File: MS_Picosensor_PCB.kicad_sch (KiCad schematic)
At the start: 24 parts, among them IC1 RASPBERRY_PI_PICO_W, J1 Conn_01x20_Socket, J2 Conn_01x20_Socket, J3 Conn_01x06_Socket, J4 Conn_01x02_Socket, J5 Conn_01x02, J6 Screw_Terminal_01x03, J7 SM04B-SRSS-TB, SW1 SW_MEC_5E, SW2 SW_MEC_5E, SW3 SW_DIP_x01

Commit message: 3v3 output
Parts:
- removed R2, R3: 1K, Resistor_THT:R_Axial_DIN0207_L6.3mm_D2.5mm_P10.16mm_Horizontal, symbol Device:R
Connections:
- net +3.3V: now also IC1.36 (3V3(OUT)), J2.5 (Pin_5); no longer IC1.37 (3V3_EN), J2.4 (Pin_4)
- new net: IC1.37 (3V3_EN), J2.4 (Pin_4)
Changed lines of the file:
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@@
-    (stroke (width 0) (type default))
-  )
-  (wire (pts (xy 132.08 125.73) (xy 132.08 128.27))
-    (stroke (width 0) (type default))
-  )
-  (wire (pts (xy 132.08 113.03) (xy 132.08 118.11))
     (stroke (width 0) (type default))
   )
@@
     (stroke (width 0) (type default))
   )
-  (wire (pts (xy 91.44 114.3) (xy 91.44 118.11))
-    (stroke (width 0) (type default))
-  )
   (wire (pts (xy 140.97 130.81) (xy 140.97 144.78))
     (stroke (width 0) (type default))
@@
     (stroke (width 0) (type default))
   )
+  (wire (pts (xy 152.4 62.23) (xy 168.91 62.23))
+    (stroke (width 0) (type default))
+  )
   (wire (pts (xy 152.4 54.61) (xy 168.91 54.61))
     (stroke (width 0) (type default))
@@
     (stroke (width 0) (type default))
   )
-  (wire (pts (xy 91.44 125.73) (xy 91.44 128.27))
-    (stroke (width 0) (type default))
-  )
   (wire (pts (xy 67.31 132.08) (xy 67.31 135.89))
     (stroke (width 0) (type default))
@@
     (stroke (width 0) (type default))
   )
-  (wire (pts (xy 152.4 62.23) (xy 168.91 62.23))
-    (stroke (width 0) (type default))
-  )
   (wire (pts (xy 29.21 31.75) (xy 29.21 35.56))
     (stroke (width 0) (type default))
@@
     (stroke (width 0) (type default))
   )
+  (wire (pts (xy 152.4 59.69) (xy 168.91 59.69))
+    (stroke (width 0) (type default))
+  )
   (wire (pts (xy 123.19 31.75) (xy 123.19 35.56))
     (stroke (width 0) (type default))
@@
     (stroke (width 0) (type default))
   )
+  (wire (pts (xy 27.94 132.08) (xy 44.45 132.08))
+    (stroke (width 0) (type default))
+  )
+  (wire (pts (xy 226.06 87.63) (xy 226.06 78.74))
+    (stroke (width 0) (type default))
+  )
+  (wire (pts (xy 36.83 80.01) (xy 53.34 80.01))
+    (stroke (width 0) (type default))
+  )
+  (wire (pts (xy 36.83 69.85) (xy 53.34 69.85))
+    (stroke (width 0) (type default))
+  )
   (wire (pts (xy 36.83 59.69) (xy 53.34 59.69))
     (stroke (width 0) (type default))
   )
-  (wire (pts (xy 27.94 132.08) (xy 44.45 132.08))
-    (stroke (width 0) (type default))
-  )
-  (wire (pts (xy 226.06 87.63) (xy 226.06 78.74))
-    (stroke (width 0) (type default))
-  )
-  (wire (pts (xy 36.83 80.01) (xy 53.34 80.01))
-    (stroke (width 0) (type default))
-  )
-  (wire (pts (xy 36.83 69.85) (xy 53.34 69.85))
-    (stroke (width 0) (type default))
-  )
   (wire (pts (xy 81.28 128.27) (xy 91.44 128.27))
     (stroke (width 0) (type default))
@@
     (stroke (width 0) (type default))
   )
-  (wire (pts (xy 152.4 59.69) (xy 168.91 59.69))
-    (stroke (width 0) (type default))
-  )
   (wire (pts (xy 152.4 97.79) (xy 168.91 97.79))
     (stroke (width 0) (type default))
@@
     (effects (font (size 1.27 1.27)) (justify left bottom))
   )
+  (label "GND" (at 36.83 95.25 0) (fields_autoplaced)
+    (effects (font (size 1.27 1.27)) (justify left bottom))
+  )
+  (label "GND" (at 36.83 57.15 0) (fields_autoplaced)
+    (effects (font (size 1.27 1.27)) (justify left bottom))
+  )
+  (label "RESET" (at 168.91 77.47 180) (fields_autoplaced)
+    (effects (font (size 1.27 1.27)) (justify right bottom))
+  )
+  (label "GND" (at 251.46 132.08 180) (fields_autoplaced)
+    (effects (font (size 1.27 1.27)) (justify right bottom))
+  )
   (label "LButton" (at 36.83 59.69 0) (fields_autoplaced)
     (effects (font (size 1.27 1.27)) (justify left bottom))
   )
-  (label "GND" (at 36.83 95.25 0) (fields_autoplaced)
-    (effects (font (size 1.27 1.27)) (justify left bottom))
-  )
-  (label "GND" (at 36.83 57.15 0) (fields_autoplaced)
-    (effects (font (size 1.27 1.27)) (justify left bottom))
-  )
-  (label "RESET" (at 168.91 77.47 180) (fields_autoplaced)
-    (effects (font (size 1.27 1.27)) (justify right bottom))
-  )
-  (label "GND" (at 251.46 132.08 180) (fields_autoplaced)
-    (effects (font (size 1.27 1.27)) (justify right bottom))
-  )
-  (label "+3.3V" (at 168.91 59.69 180) (fields_autoplaced)
-    (effects (font (size 1.27 1.27)) (justify right bottom))
-  )
   (label "GND" (at 104.14 165.1 180) (fields_autoplaced)
     (effects (font (size 1.27 1.27)) (justify right bottom))
@@
   (label "GLED" (at 27.94 118.11 0) (fields_autoplaced)
     (effects (font (size 1.27 1.27)) (justify left bottom))
+  )
+  (label "+3.3V" (at 168.91 62.23 180) (fields_autoplaced)
+    (effects (font (size 1.27 1.27)) (justify right bottom))
   )
   (symbol (lib_id "Connector:Conn_01x20_Socket") (at 31.75 74.93 0) (mirror y) (unit 1)
@@
     )
   )
-  (symbol (lib_id "power:+3.3V") (at 132.08 113.03 0) (unit 1)
-    (in_bom yes) (on_board yes) (dnp no) (fields_autoplaced)
-    (property "Reference" "#PWR07" (at 132.08 116.84 0)
-      (effects (font (size 1.27 1.27)) hide)
-    )
-    (property "Value" "+3.3V" (at 132.08 107.95 0)
-      (effects (font (size 1.27 1.27)))
-    )
-    (property "Footprint" "" (at 132.08 113.03 0)
-      (effects (font (size 1.27 1.27)) hide)
-    )
-    (property "Datasheet" "" (at 132.08 113.03 0)
-      (effects (font (size 1.27 1.27)) hide)
-    )
-    (pin "1")
-    (instances
-      (project "MS_Picosensor_PCB"
-        (path "/5da62d0f-f29a-4905-9ab2-b5107813951f"
-          (reference "#PWR07") (unit 1)
-        )
-      )
-    )
-  )
   (symbol (lib_id "Device:R") (at 48.26 132.08 90) (unit 1)
     (in_bom yes) (on_board yes) (dnp no) (fields_autoplaced)
@@
         (path "/5da62d0f-f29a-4905-9ab2-b5107813951f"
           (reference "#PWR012") (unit 1)
-        )
-      )
-    )
-  )
-  (symbol (lib_id "Device:R") (at 132.08 121.92 0) (unit 1)
-    (in_bom yes) (on_board yes) (dnp no) (fields_autoplaced)
-    (property "Reference" "R3" (at 134.62 120.65 0)
-      (effects (font (size 1.27 1.27)) (justify left))
-    )
-    (property "Value" "1K" (at 134.62 123.19 0)
-      (effects (font (size 1.27 1.27)) (justify left))
-    )
-    (property "Footprint" "Resistor_THT:R_Axial_DIN0207_L6.3mm_D2.5mm_P10.16mm_Horizontal" (at 130.302 121.92 90)
-      (effects (font (size 1.27 1.27)) hide)
-    )
-    (property "Datasheet" "~" (at 132.08 121.92 0)
-      (effects (font (size 1.27 1.27)) hide)
-    )
-    (pin "1")
-    (pin "2")
-    (instances
-      (project "MS_Picosensor_PCB"
-        (path "/5da62d0f-f29a-4905-9ab2-b5107813951f"
-          (reference "R3") (unit 1)
         )
       )
@@
     )
   )
-  (symbol (lib_id "power:+3.3V") (at 91.44 114.3 0) (unit 1)
-    (in_bom yes) (on_board yes) (dnp no) (fields_autoplaced)
-    (property "Reference" "#PWR06" (at 91.44 118.11 0)
-      (effects (font (size 1.27 1.27)) hide)
-    )
-    (property "Value" "+3.3V" (at 91.44 109.22 0)
-      (effects (font (size 1.27 1.27)))
-    )
-    (property "Footprint" "" (at 91.44 114.3 0)
-      (effects (font (size 1.27 1.27)) hide)
-    )
-    (property "Datasheet" "" (at 91.44 114.3 0)
-      (effects (font (size 1.27 1.27)) hide)
-    )
-    (pin "1")
-    (instances
-      (project "MS_Picosensor_PCB"
-        (path "/5da62d0f-f29a-4905-9ab2-b5107813951f"
-          (reference "#PWR06") (unit 1)
-        )
-      )
-    )
-  )
   (symbol (lib_id "power:GND") (at 97.79 146.05 0) (unit 1)
     (in_bom yes) (on_board yes) (dnp no) (fields_autoplaced)
@@
         )
       )
-    )
-  )
-  (symbol (lib_id "Device:R") (at 91.44 121.92 0) (unit 1)
-    (in_bom yes) (on_board yes) (dnp no) (fields_autoplaced)
-    (property "Reference" "R2" (at 93.98 120.65 0)
-      (effects (font (size 1.27 1.27)) (justify left))
-    )
-    (property "Value" "1K" (at 93.98 123.19 0)
-      (effects (font (size 1.27 1.27)) (justify left))
-    )
-    (property "Footprint" "Resistor_THT:R_Axial_DIN0207_L6.3mm_D2.5mm_P10.16mm_Horizontal" (at 89.662 121.92 90)
-      (effects (font (size 1.27 1.27)) hide)
-    )
-    (property "Datasheet" "~" (at 91.44 121.92 0)
-      (effects (font (size 1.27 1.27)) hide)
-    )
-    (pin "1")
-    (pin "2")
-    (instances
-      (project "MS_Picosensor_PCB"
-        (path "/5da62d0f-f29a-4905-9ab2-b5107813951f"
-          (reference "R2") (unit 1)
-        )
-      )

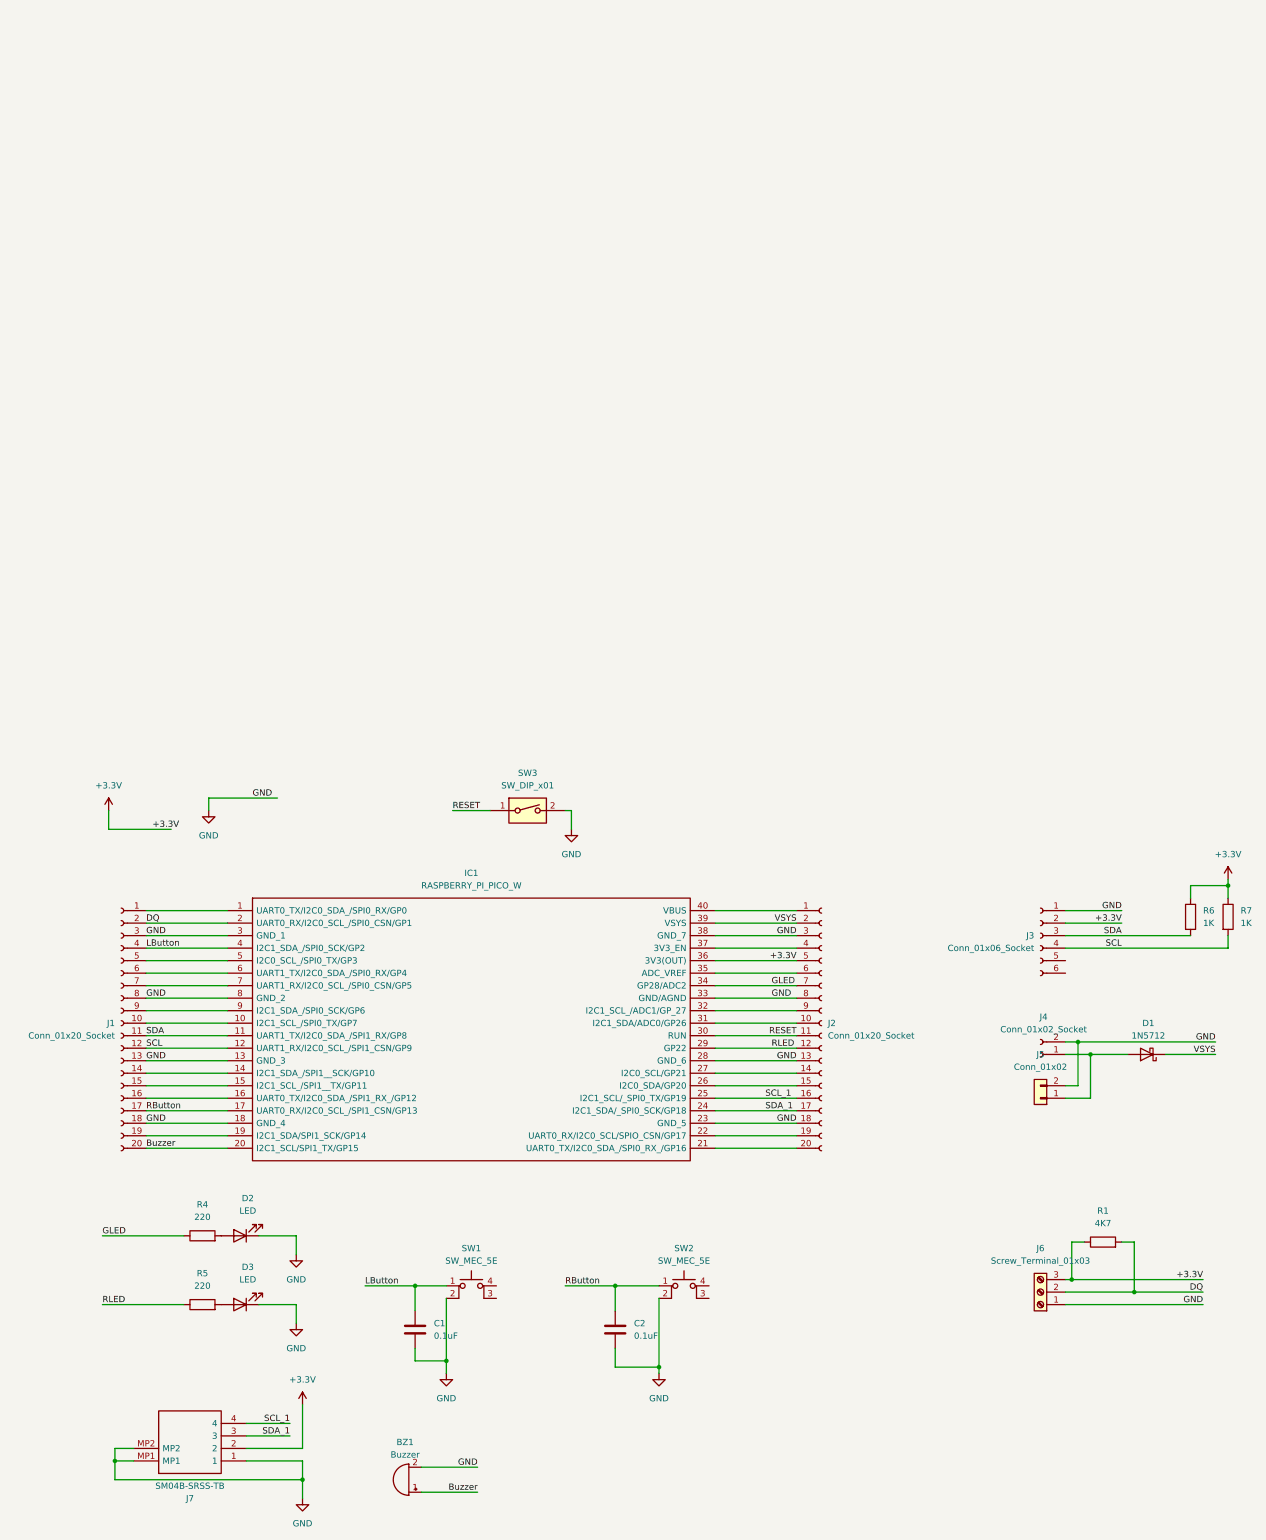
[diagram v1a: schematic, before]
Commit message: add part for smd
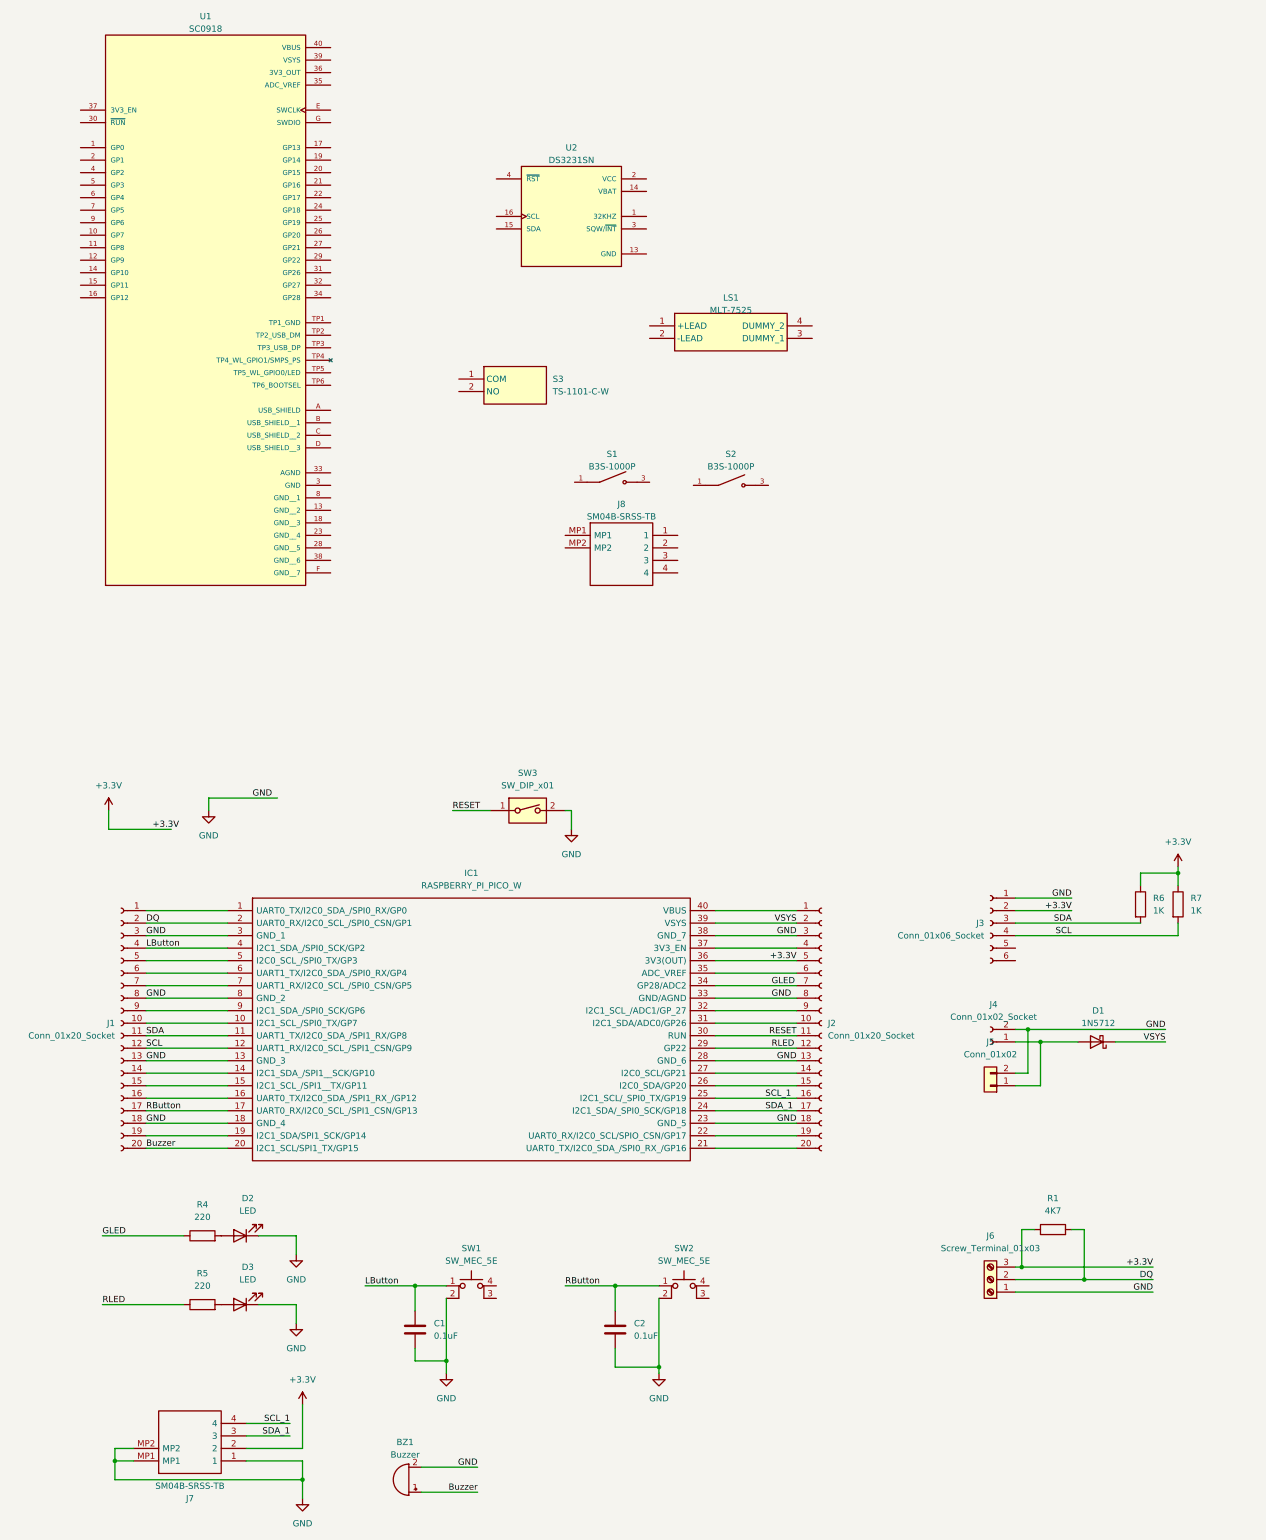
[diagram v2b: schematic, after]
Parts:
- added J8: SM04B-SRSS-TB, SM04BSRSSTB, symbol SM04B-SRSS-TB:SM04B-SRSS-TB
- added LS1: MLT-7525, MLT7525, symbol MLT-7525:MLT-7525
- added S1, S2: B3S-1000P, B3S-1000P:SW_B3S-1000P, symbol B3S-1000P:B3S-1000P
- added S3: TS-1101-C-W, TS1101CW, symbol TS-1101-C-W:TS-1101-C-W
- added U1: SC0918, SC0918:MODULE_SC0918, symbol SC0918:SC0918
- added U2: DS3231SN, DS3231SN:SOIC127P1032X265-16N, symbol DS3231SN:DS3231SN
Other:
- title: (none) -> DataPi
- moved on the sheet: D1, J3, J4, J5, J6, R1, R6, R7
